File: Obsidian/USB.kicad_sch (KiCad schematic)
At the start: 40 parts, among them J2 USB_C_Receptacle_USB2.0_16P, U21 FT2232HQ, U22 93LC46B_SN, U8 TLV62565DBV, Y5 X503212MSB2GI

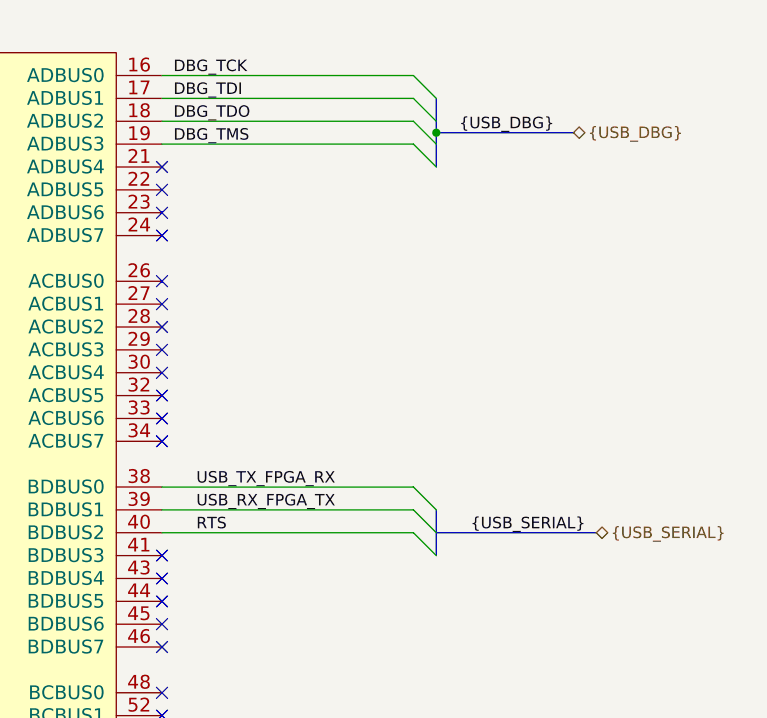
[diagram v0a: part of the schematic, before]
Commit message: check USB serial signals : Continuous plane OK, ground via whenever possible
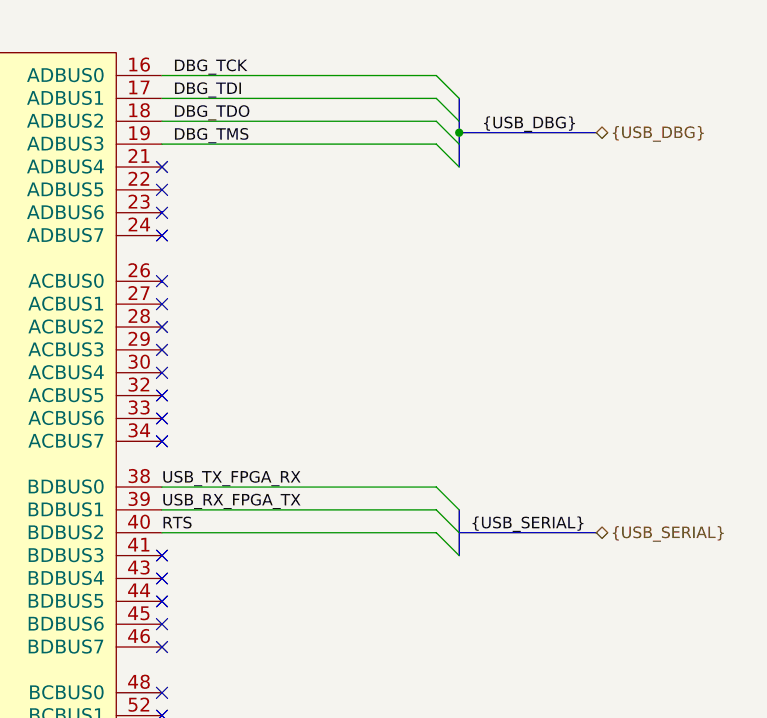
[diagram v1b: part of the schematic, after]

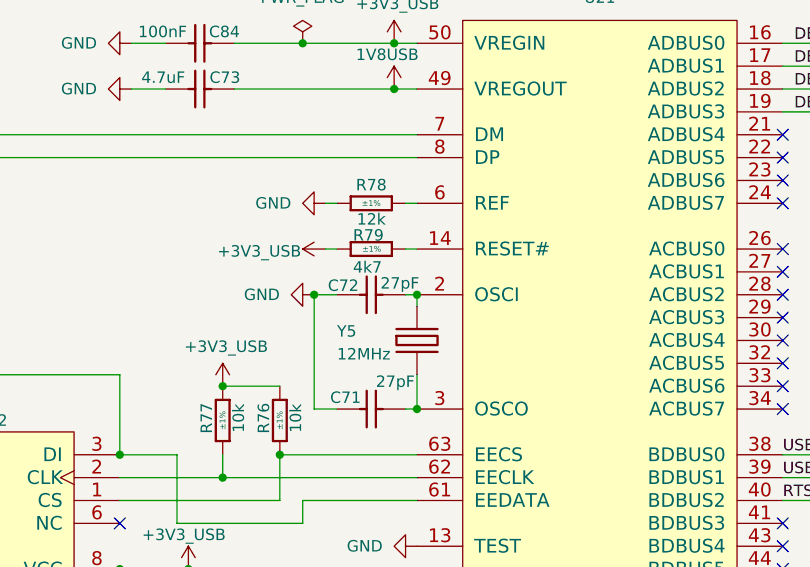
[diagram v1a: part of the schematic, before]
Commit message: replacing FH 0402CG270J500NT capacitor for XTAL in USB with CL05C330JB5NNNC
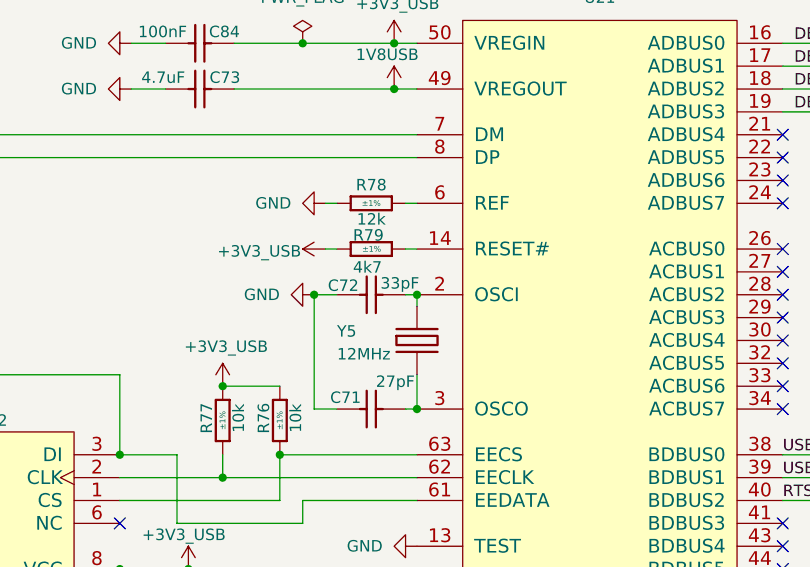
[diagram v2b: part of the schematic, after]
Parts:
- C72: value CC0402_27PF_50V_5%_C0G -> CC0402_33PF_50V_5%_C0G; LCSC C1557 -> C70465; Manufacturer Part Number CC0402_27PF_50V_5%_C0G -> CC0402_33PF_50V_5%_C0G; Manufacturer1 Example KEMET -> Samsung Electro-Mechanics; Manufacturer1 Part Number C0402C270J5GACTU -> CL05C330JB5NNNC; Val 27pF -> 33pF
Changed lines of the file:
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@@
 			)
 		)
-		(property "Value" "CC0402_27PF_50V_5%_C0G"
+		(property "Value" "CC0402_33PF_50V_5%_C0G"
 			(at 180.34 50.927 0)
 			(effects
@@
 			)
 		)
-		(property "Val" "27pF"
+		(property "Val" "33pF"
 			(at 177.546 55.88 0)
 			(effects
@@
 			)
 		)
-		(property "Manufacturer Part Number" "CC0402_27PF_50V_5%_C0G"
+		(property "Manufacturer Part Number" "CC0402_33PF_50V_5%_C0G"
 			(at 180.34 12.827 0)
 			(effects
@@
 			)
 		)
-		(property "Manufacturer1 Example" "KEMET"
+		(property "Manufacturer1 Example" "Samsung Electro-Mechanics"
 			(at 180.34 -4.318 0)
 			(effects
@@
 			)
 		)
-		(property "Manufacturer1 Part Number" "C0402C270J5GACTU"
+		(property "Manufacturer1 Part Number" "CL05C330JB5NNNC"
 			(at 180.34 -6.223 0)
 			(effects
@@
 			)
 		)
-		(property "LCSC" "C1557"
+		(property "LCSC" "C70465"
 			(at 180.34 57.15 0)
 			(effects

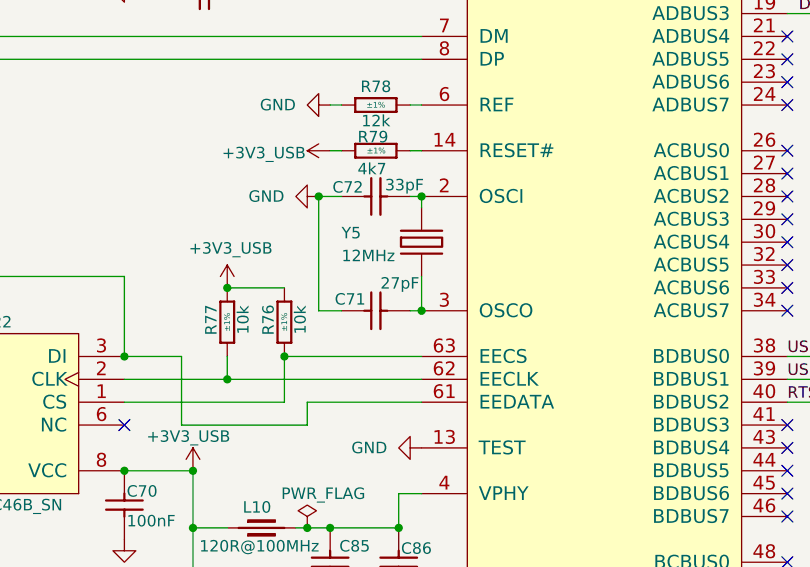
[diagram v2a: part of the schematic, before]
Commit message: correcting straightness of kicad plane around 1V2 regulator
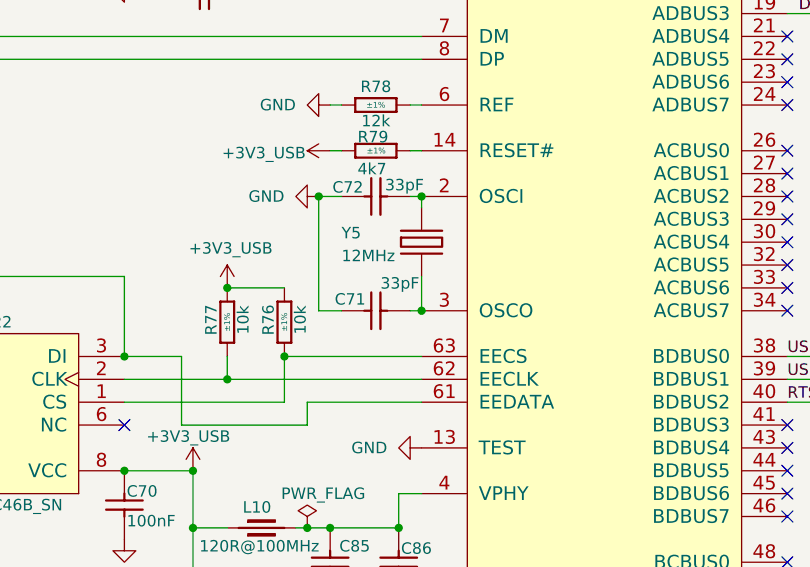
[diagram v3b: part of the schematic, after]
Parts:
- C71: value CC0402_27PF_50V_5%_C0G -> CC0402_33PF_50V_5%_C0G; Comment 27pF -> 33pF; LCSC C1557 -> C70465; Manufacturer Part Number CC0402_27PF_50V_5%_C0G -> CC0402_33PF_50V_5%_C0G; Manufacturer1 Example KEMET -> Samsung Electro-Mechanics; Manufacturer1 Part Number C0402C270J5GACTU -> CL05C330JB5NNNC; Part Number CC0402_27PF_50V_5%_C0G -> CC0402_33PF_50V_5%_C0G; Val 27pF -> 33pF
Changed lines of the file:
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@@
 			)
 		)
-		(property "Value" "CC0402_27PF_50V_5%_C0G"
+		(property "Value" "CC0402_33PF_50V_5%_C0G"
 			(at 180.34 63.627 0)
 			(effects
@@
 			)
 		)
-		(property "Val" "27pF"
+		(property "Val" "33pF"
 			(at 177.038 66.802 0)
 			(effects
@@
 			)
 		)
-		(property "Part Number" "CC0402_27PF_50V_5%_C0G"
+		(property "Part Number" "CC0402_33PF_50V_5%_C0G"
 			(at 180.34 57.912 0)
 			(effects
@@
 			)
 		)
-		(property "Comment" "27pF"
+		(property "Comment" "33pF"
 			(at 180.34 52.197 0)
 			(effects
@@
 			)
 		)
-		(property "Manufacturer Part Number" "CC0402_27PF_50V_5%_C0G"
+		(property "Manufacturer Part Number" "CC0402_33PF_50V_5%_C0G"
 			(at 180.34 25.527 0)
 			(effects
@@
 			)
 		)
-		(property "Manufacturer1 Example" "KEMET"
+		(property "Manufacturer1 Example" "Samsung Electro-Mechanics"
 			(at 180.34 8.382 0)
 			(effects
@@
 			)
 		)
-		(property "Manufacturer1 Part Number" "C0402C270J5GACTU"
+		(property "Manufacturer1 Part Number" "CL05C330JB5NNNC"
 			(at 180.34 6.477 0)
 			(effects
@@
 			)
 		)
-		(property "LCSC" "C1557"
+		(property "LCSC" "C70465"
 			(at 180.34 69.85 0)
 			(effects

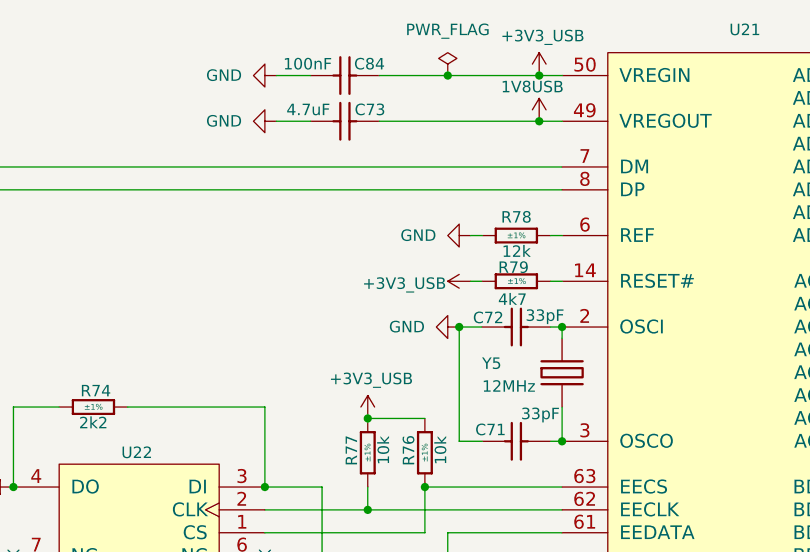
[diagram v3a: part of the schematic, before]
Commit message: Modifying line voltage for certain components, adding pull up resistor
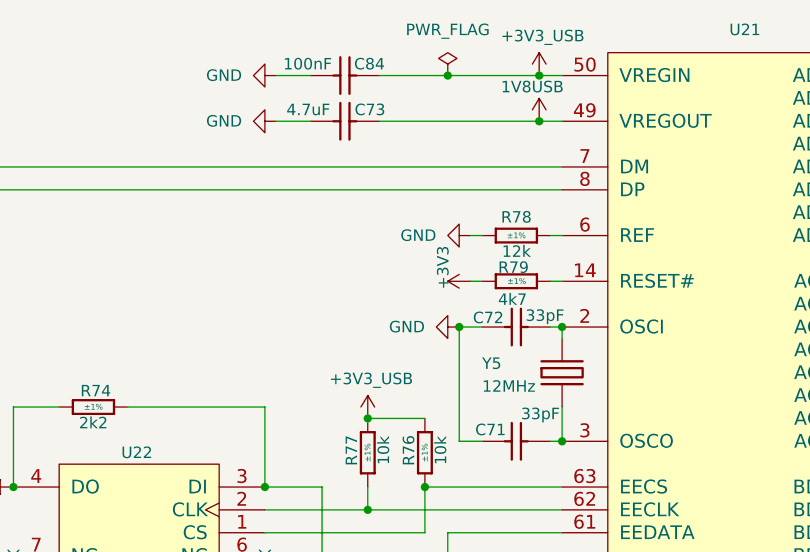
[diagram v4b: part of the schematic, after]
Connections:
- net +3V3: now also R79.2
- net +3V3_USB: no longer R79.2
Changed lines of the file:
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@@
 	(symbol
 		(lib_id "Library_Symbol:+3V3_USB")
-		(at 171.45 52.07 90)
-		(unit 1)
-		(exclude_from_sim no)
-		(in_bom yes)
-		(on_board yes)
-		(dnp no)
-		(property "Reference" "#PWR0107"
-			(at 175.26 52.07 0)
-			(effects
-				(font
-					(size 1.27 1.27)
-				)
-				(hide yes)
-			)
-		)
-		(property "Value" "+3V3_USB"
-			(at 164.084 52.324 90)
-			(effects
-				(font
-					(size 1.27 1.27)
-				)
-			)
-		)
-		(property "Footprint" ""
-			(at 171.45 52.07 0)
-			(effects
-				(font
-					(size 1.27 1.27)
-				)
-				(hide yes)
-			)
-		)
-		(property "Datasheet" ""
-			(at 171.45 52.07 0)
-			(effects
-				(font
-					(size 1.27 1.27)
-				)
-				(hide yes)
-			)
-		)
-		(property "Description" ""
-			(at 171.45 52.07 0)
-			(effects
-				(font
-					(size 1.27 1.27)
-				)
-				(hide yes)
-			)
-		)
-		(pin "1"
-		)
-		(instances
-			(project "Marble_Tiny"
-				(path "/c2a4f786-b14c-434a-acf7-b20fb2221b0b/62565c75-62b0-4544-832f-1275174835af"
-					(reference "#PWR0107")
-					(unit 1)
-				)
-			)
-		)
-	)
-	(symbol
-		(lib_id "Library_Symbol:+3V3_USB")
 		(at 156.21 87.63 0)
 		(unit 1)
@@
 					(unit 1)
 				)
+			)
+		)
+	)
+	(symbol
+		(lib_id "Library_Symbol:+1V0")
+		(at 171.45 52.07 90)
+		(unit 1)
+		(exclude_from_sim no)
+		(in_bom yes)
+		(on_board yes)
+		(dnp no)
+		(property "Reference" "#PWR061"
+			(at 175.26 52.07 0)
+			(effects
+				(font
+					(size 1.27 1.27)
+				)
+				(hide yes)
+			)
+		)
+		(property "Value" "+3V3"
+			(at 168.402 50.546 0)
+			(effects
+				(font
+					(size 1.27 1.27)
+				)
+			)
+		)
+		(property "Footprint" ""
+			(at 171.45 52.07 0)
+			(effects
+				(font
+					(size 1.27 1.27)
+				)
+				(hide yes)
+			)
+		)
+		(property "Datasheet" ""
+			(at 171.45 52.07 0)
+			(effects
+				(font
+					(size 1.27 1.27)
+				)
+				(hide yes)
+			)
+		)
+		(property "Description" "Power symbol creates a global label with name \"+1V0\""
+			(at 171.45 52.07 0)
+			(effects
+				(font
+					(size 1.27 1.27)
+				)
+				(hide yes)
+			)
+		)
+		(pin "1"
+		)
+		(instances
+			(project "Obsidian"
+				(path "/c2a4f786-b14c-434a-acf7-b20fb2221b0b/62565c75-62b0-4544-832f-1275174835af"
+					(reference "#PWR061")
+					(unit 1)
+				)

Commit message: update LCSC reference, and OFFSET rotation for JLCPCB
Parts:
- U22: FT Rotation Offset (none) -> 270
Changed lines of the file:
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@@
 			)
 		)
-		(property "FT Rotation Offset" ""
+		(property "FT Rotation Offset" "270"
 			(at 143.51 72.39 0)
 			(effects

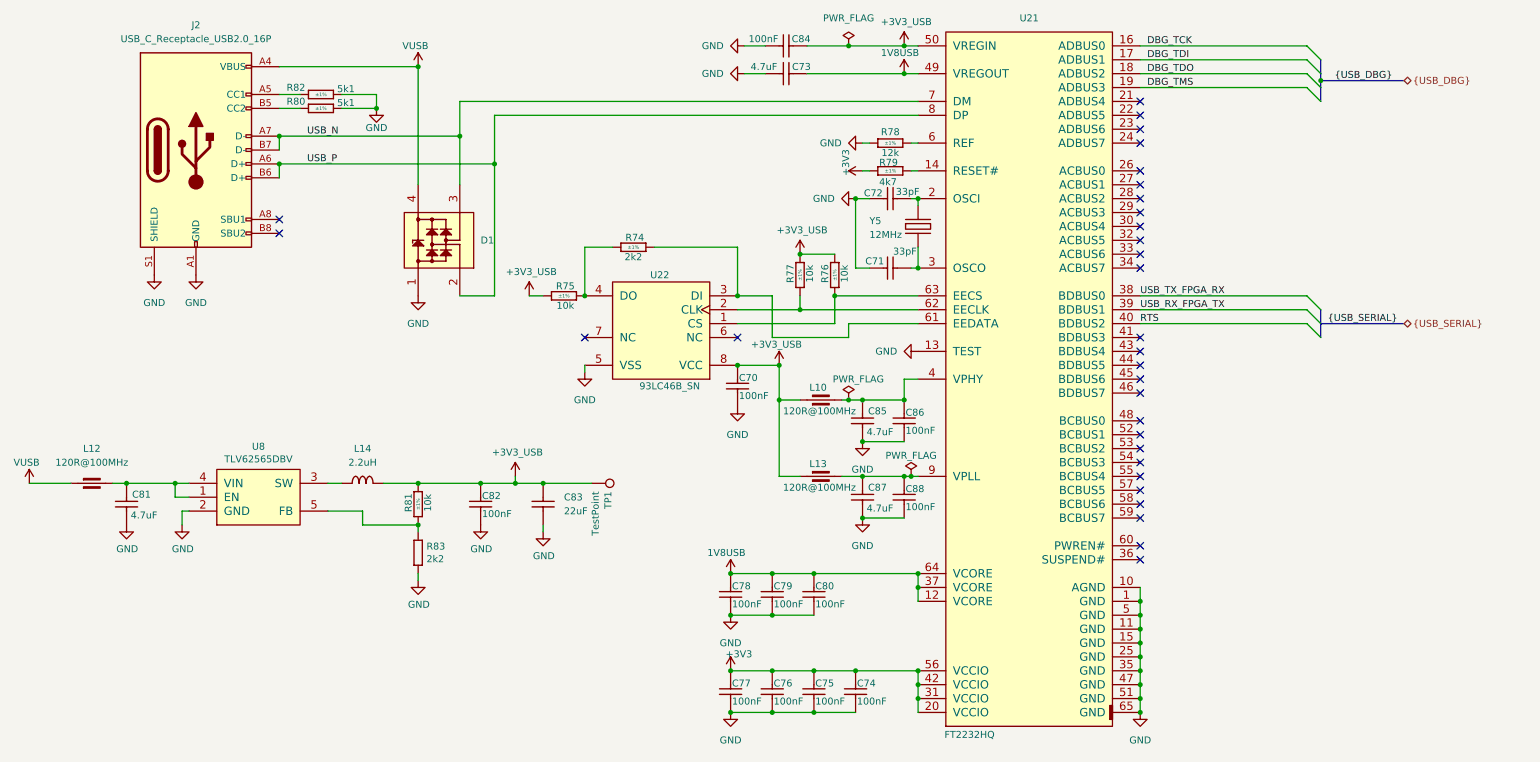
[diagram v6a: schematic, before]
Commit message: Adding documentation for configuration with flash memory, adding more comments to schematic
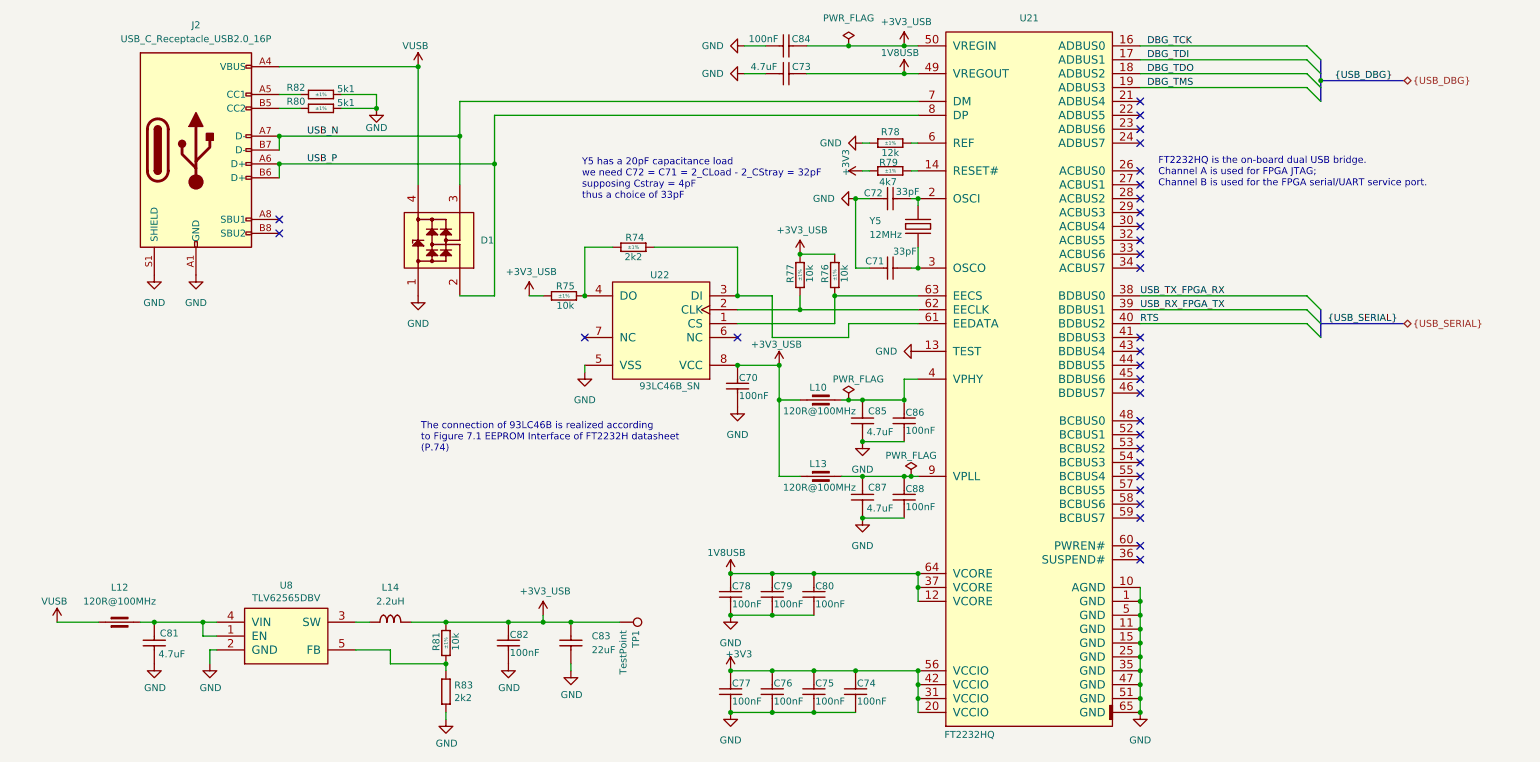
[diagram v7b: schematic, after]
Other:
- note added: "FT2232HQ is the on-board dual USB bridge. Channel A is used for FPGA JTAG; Channel B is used for the FPGA serial/UART service port."
- note added: "The connection of 93LC46B is realized according to Figure 7.1 EEPROM Interface of FT2232H datasheet (P.74)"
- note added: "Y5 has a 20pF capacitance load we need C72 = C71 = 2_CLoad - 2_CStray = 32pF supposing Cstray = 4pF thus a choice of 33pF"
- moved on the sheet: C81, C82, C83, L12, L14, R81, R83, TP1, U8

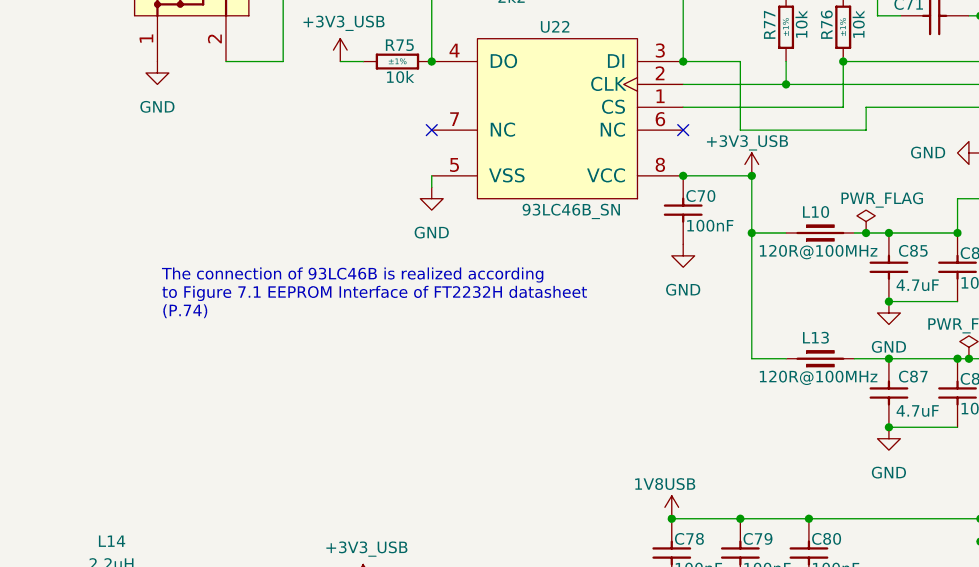
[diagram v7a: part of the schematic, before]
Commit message: adding comments, and test point for U12 (power supply in clock sheet)
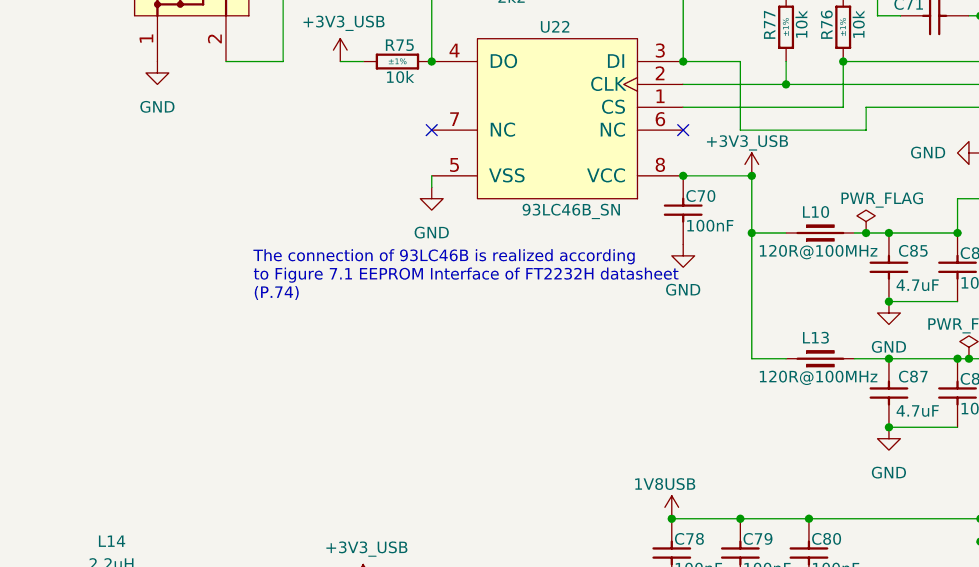
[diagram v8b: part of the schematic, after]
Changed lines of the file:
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@@
 	(text "The connection of 93LC46B is realized according \nto Figure 7.1 EEPROM Interface of FT2232H datasheet\n(P.74)"
 		(exclude_from_sim no)
-		(at 90.678 100.838 0)
+		(at 100.838 98.806 0)
 		(effects
 			(font
